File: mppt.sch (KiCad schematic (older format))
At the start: 9 parts, among them P101 CONN_01X02, P102 CONN_01X02, P103 JTAG, P104 CONN_01X02, U102 STM32F103C8Tx, U104 SN65HVD12DR

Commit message: Changed a bit, and did a full re-route
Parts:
- removed U104: SN65HVD12DR, Housings_SOIC:SOIJ-8_5.3x5.3mm_Pitch1.27mm, symbol SN65HVD12DR
- added U101: ST3485ECDR, Housings_SOIC:SOIC-8_3.9x4.9mm_Pitch1.27mm, symbol ST3485ECDR
- P103: footprint Pin_Headers:Pin_Header_Straight_2x10 -> lib:20p_edge
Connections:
- net labels added: Iin
- wire segments 46 -> 45
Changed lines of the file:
@@
 F 0 "P103" H 15325 1975 50  0000 C CNN
 F 1 "JTAG" H 15325 875 50  0000 C CNN
-F 2 "Pin_Headers:Pin_Header_Straight_2x10" H 15325 225 50  0001 C CNN
+F 2 "lib:20p_edge" H 15325 225 50  0001 C CNN
 F 3 "" H 15325 225 50  0000 C CNN
 	1    15325 1425
@@
 $EndSheet
 Wire Wire Line
-	10375 7975 10975 7975
-Wire Wire Line
-	10975 7975 10975 5200
-Wire Wire Line
-	10975 5200 8875 5200
+	11425 5200 8875 5200
 Wire Wire Line
 	8875 5025 11000 5025
@@
 Wire Wire Line
 	4950 4250 5425 4250
-$Comp
-L SN65HVD12DR U104
-U 1 1 58535CA2
-P 13875 9225
-F 0 "U104" H 13875 10175 118 0000 C CNN
-F 1 "SN65HVD12DR" H 13975 8525 118 0000 C CNN
-F 2 "Housings_SOIC:SOIJ-8_5.3x5.3mm_Pitch1.27mm" H 13525 9225 118 0001 C CNN
-F 3 "" H 13525 9225 118 0001 C CNN
-F 4 "2436744" H 13975 10275 118 0001 C CNN "farnell"
-	1    13875 9225
-	1    0    0    -1
-$EndComp
-Wire Wire Line
-	10375 8875 12725 8875
+Wire Wire Line
+	10375 8875 12625 8875
 Wire Wire Line
 	10375 8975 13275 8975
@@
 	1    0    0    -1
 $EndComp
-$Comp
-L +5V #PWR010
-U 1 1 5857A021
-P 13875 8675
-F 0 "#PWR010" H 13875 8525 50  0001 C CNN
-F 1 "+5V" H 13875 8815 50  0000 C CNN
-F 2 "" H 13875 8675 50  0000 C CNN
-F 3 "" H 13875 8675 50  0000 C CNN
-	1    13875 8675
-	1    0    0    -1
-$EndComp
 Wire Wire Line
 	13275 9425 13175 9425
 Wire Wire Line
-	13175 9425 12725 8875
+	13175 9425 12625 8875
 $Comp
 L C C101
@@
 	2250 7000 2800 7000
 Wire Wire Line
-	2800 7300 2250 7300
+	2250 7300 2800 7300
 $Comp
 L C C102
@@
 Connection ~ 2525 7000
 $Comp
-L GND #PWR011
+L GND #PWR010
 U 1 1 5857CB62
 P 2525 7300
-F 0 "#PWR011" H 2525 7050 50  0001 C CNN
+F 0 "#PWR010" H 2525 7050 50  0001 C CNN
 F 1 "GND" H 2525 7150 50  0000 C CNN
 F 2 "" H 2525 7300 50  0000 C CNN
@@
 $EndComp
 $Comp
-L +3V3 #PWR012
+L +3V3 #PWR011
 U 1 1 5857CBBE
 P 2525 7000
-F 0 "#PWR012" H 2525 6850 50  0001 C CNN
+F 0 "#PWR011" H 2525 6850 50  0001 C CNN
 F 1 "+3V3" H 2525 7140 50  0000 C CNN
 F 2 "" H 2525 7000 50  0000 C CNN
@@
 	1    0    0    -1
 $EndComp
+Text Label 11250 5200 0    60   ~ 0
+Iin
+Text Label 4275 8075 0    60   ~ 0
+Iin
+Wire Wire Line
+	4275 8075 4575 8075
+$Comp
+L ST3485ECDR U101
+U 1 1 585FCDC0
+P 13875 9225
+F 0 "U101" H 13875 10175 118 0000 C CNN
+F 1 "ST3485ECDR" H 13975 8525 118 0000 C CNN
+F 2 "Housings_SOIC:SOIC-8_3.9x4.9mm_Pitch1.27mm" H 13525 9225 118 0001 C CNN
+F 3 "" H 13525 9225 118 0001 C CNN
+F 4 "1842628" H 13975 10275 118 0001 C CNN "farnell"
+	1    13875 9225
+	1    0    0    -1
+$EndComp
+$Comp
+L +3V3 #PWR012
+U 1 1 585FCF35
+P 13875 8675
+F 0 "#PWR012" H 13875 8525 50  0001 C CNN
+F 1 "+3V3" H 13875 8815 50  0000 C CNN
+F 2 "" H 13875 8675 50  0000 C CNN
+F 3 "" H 13875 8675 50  0000 C CNN
+	1    13875 8675
+	1    0    0    -1
+$EndComp

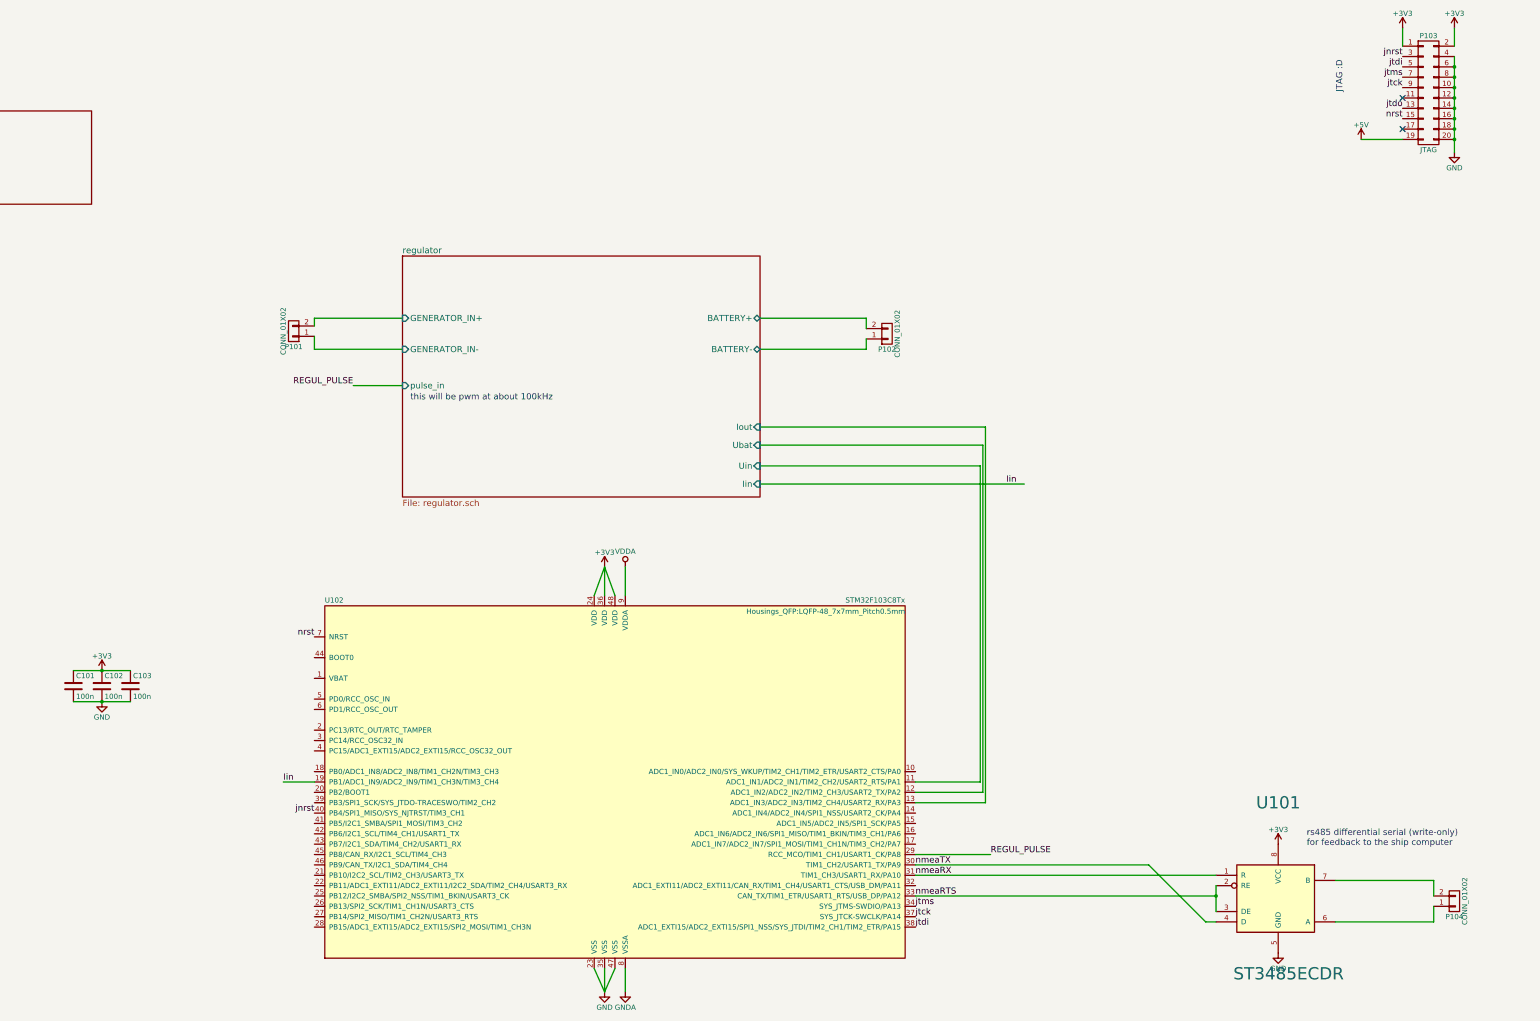
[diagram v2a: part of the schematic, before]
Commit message: Rerouted, and made everything beautifull
 - added screw bolt-holes for the output.
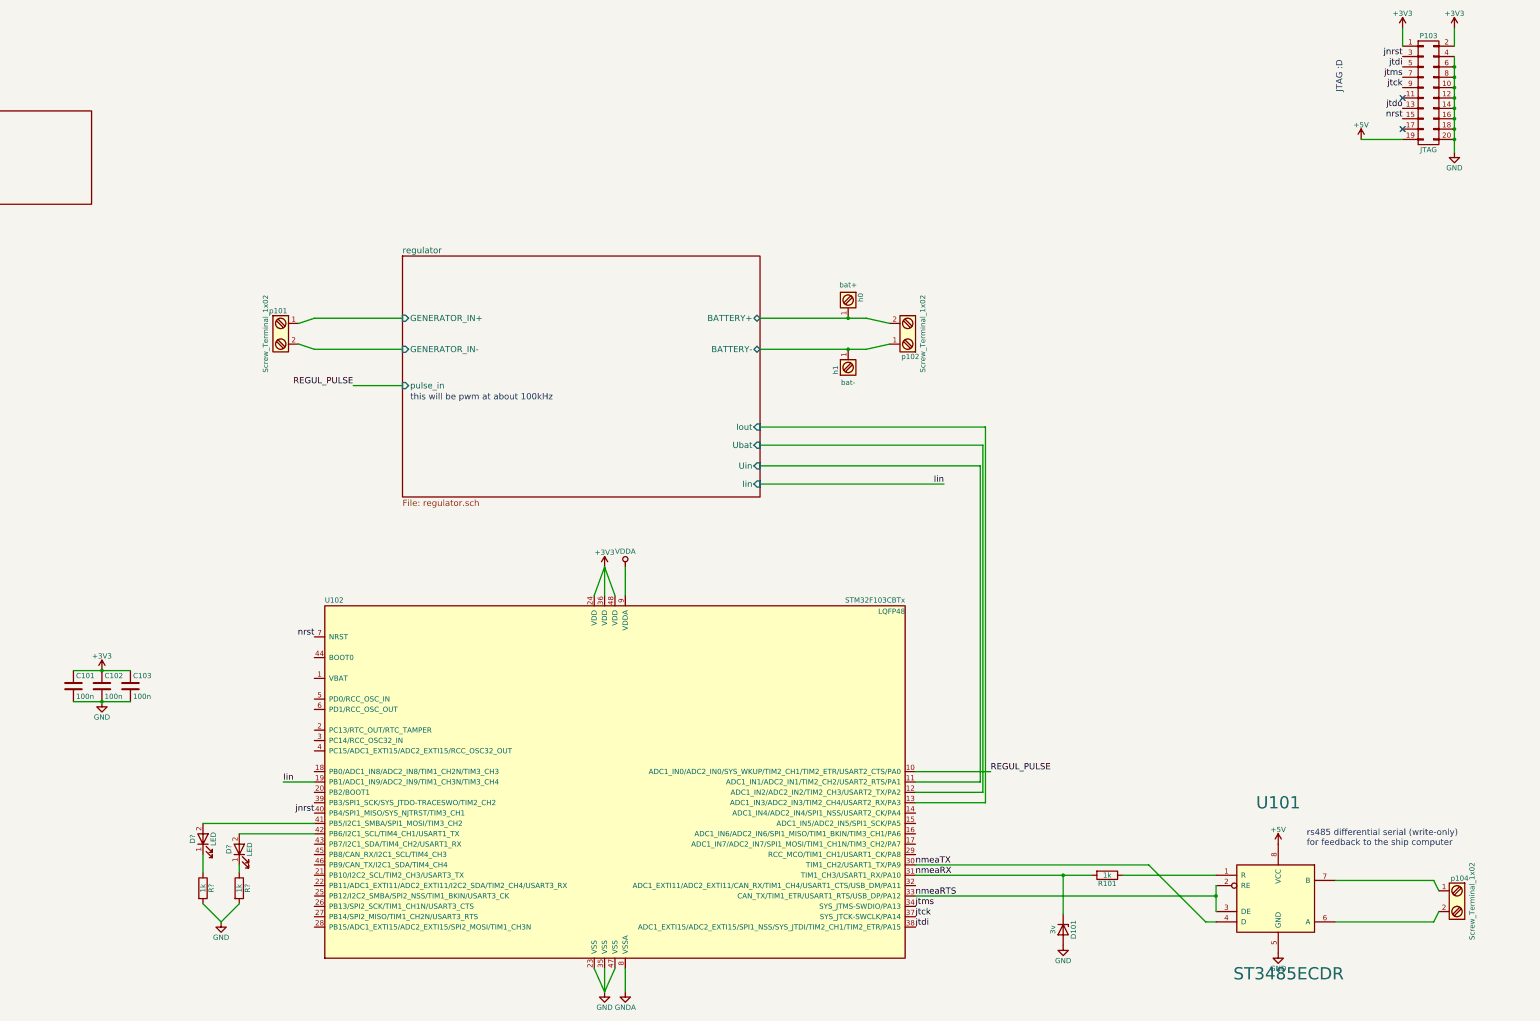
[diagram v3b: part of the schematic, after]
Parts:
- removed P101, P102, P104: CONN_01X02, Pin_Headers:Pin_Header_Straight_1x02, symbol CONN_01X02
- removed U102: STM32F103C8Tx, Housings_QFP:LQFP-48_7x7mm_Pitch0.5mm, symbol STM32F103C8Tx
- added D101: 3v, Diodes_SMD:D_SOD-323_HandSoldering, symbol D_Zener
- added D? (x2): LED, symbol LED
- added R101: 1k, Resistors_SMD:R_0805, symbol R
- added R? (x2): 1k, symbol R
- added U102: STM32F103CBTx, LQFP48, symbol STM32F103CBTx
- added h0: bat+, lib:m4_hole, symbol Screw_Terminal_1x01
- added h1: bat-, lib:m4_hole, symbol Screw_Terminal_1x01
- added p101, p102, p104: Screw_Terminal_1x02, lib:terminal, symbol Screw_Terminal_1x02
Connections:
- net +3V3: now also U102.24 (VDD), U102.36 (VDD), U102.48 (VDD); no longer U101.8 (VCC)
- net +5V: now also U101.8 (VCC)
- net GND: now also D101.2 (A), R?.2, R?.2, U102.23 (VSS), U102.35 (VSS), U102.47 (VSS)
- net GNDA: now also U102.8 (VSSA)
- net Iin: now also U102.19 (PB1/ADC1_IN9/ADC2_IN9/TIM1_CH3N/TIM3_CH4)
- net REGUL_PULSE: now also U102.10 (ADC1_IN0/ADC2_IN0/SYS_WKUP/TIM2_CH1/TIM2_ETR/USART2_CTS/PA0)
- net VDDA: now also U102.9 (VDDA)
- net jnrst: now also U102.40 (PB4/SPI1_MISO/SYS_NJTRST/TIM3_CH1)
- net jtck: now also U102.37 (SYS_JTCK-SWCLK/PA14)
- net jtdi: now also U102.38 (ADC1_EXTI15/ADC2_EXTI15/SPI1_NSS/SYS_JTDI/TIM2_CH1/TIM2_ETR/PA15)
- net jtms: now also U102.34 (SYS_JTMS-SWDIO/PA13)
- net nmeaRTS: now also U102.33 (CAN_TX/TIM1_ETR/USART1_RTS/USB_DP/PA12)
- net nmeaRX: now also D101.1 (K), R101.2, U102.31 (TIM1_CH3/USART1_RX/PA10); no longer U101.1 (R)
- net nmeaTX: now also U102.30 (TIM1_CH2/USART1_TX/PA9)
- net nrst: now also U102.7 (NRST)
- net regulator/BATTERY+: now also h0.1, p102.2
- net regulator/BATTERY-: now also h1.1, p102.1
- net regulator/GENERATOR_IN+: now also p101.1
- net regulator/GENERATOR_IN-: now also p101.2
- net regulator/Iout: now also U102.13 (ADC1_IN3/ADC2_IN3/TIM2_CH4/USART2_RX/PA3)
- net regulator/Ubat: now also U102.12 (ADC1_IN2/ADC2_IN2/TIM2_CH3/USART2_TX/PA2)
- net regulator/Uin: now also U102.11 (ADC1_IN1/ADC2_IN1/TIM2_CH2/USART2_RTS/PA1)
- net at U101.6 (A): now also p104.2
- net at U101.7 (B): now also p104.1
- new net: R101.1, U101.1 (R)
- new net: D?.2 (A), U102.41 (PB5/I2C1_SMBA/SPI1_MOSI/TIM3_CH2)
- new net: D?.2 (A), U102.42 (PB6/I2C1_SCL/TIM4_CH1/USART1_TX)
- new net: D?.1 (K), R?.1 (x2)

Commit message: Added small display.
And made everything look even nicer
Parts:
- removed D? (x2): LED, symbol LED
- removed P103: JTAG, lib:20p_edge, symbol CONN_02X10
- removed R? (x2): 1k, symbol R
- added J101: CONN_01X05, mylibs:swd_conn, symbol CONN_01X05
- U102: footprint LQFP48 -> Housings_QFP:LQFP-48_7x7mm_Pitch0.5mm
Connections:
- net +3V3: now also J101.5 (P5)
- net GND: now also J101.1 (P1)
- net nrst: now also J101.2 (P2)
- net leds/inB: now reaches U102.39 (PB3/SPI1_SCK/SYS_JTDO-TRACESWO/TIM2_CH2)
- net leds/in1: now reaches U102.41 (PB5/I2C1_SMBA/SPI1_MOSI/TIM3_CH2)
- net leds/in2: now reaches U102.42 (PB6/I2C1_SCL/TIM4_CH1/USART1_TX)
- net leds/in3: now reaches U102.43 (PB7/I2C1_SDA/TIM4_CH2/USART1_RX)
- net leds/in4: now reaches U102.45 (PB8/CAN_RX/I2C1_SCL/TIM4_CH3)
- net leds/inA: now reaches U102.46 (PB9/CAN_TX/I2C1_SDA/TIM4_CH4)
- net jtck renamed swclk
- net swclk: now also J101.3 (P3)
- net jtdi renamed leds/inC
- net jtms renamed swdio
- net swdio: now also J101.4 (P4)
- no-connect marks 2 -> 0
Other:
- note removed: "JTAG :D"
